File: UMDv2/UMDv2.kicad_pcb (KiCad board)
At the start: 2 copper layers, 130.8 x 83.8 mm, 112 parts, among them CON201 USB-B1HSB6, CON302 JTAG-2X10-HDR, CON303 101-00405-75, CON304 UMDv2-CONN, CON305 HDR1X2, CON306 HDR1X3, SW301 PTS645SM43SMTR92_LFS, U201 MIC5504-3.3YM5-TR, U202 TPS2115APWR, U203 TPS25921ADR, U205 AZ1117CH-3.3TRG1, U207 INA199A2DCKR, U301 STM32F413ZHT6, U302 74ALVC164245DL,118, U303 74ALVC164245DL,118, X301 ECS-80-18-30-JGN-TR

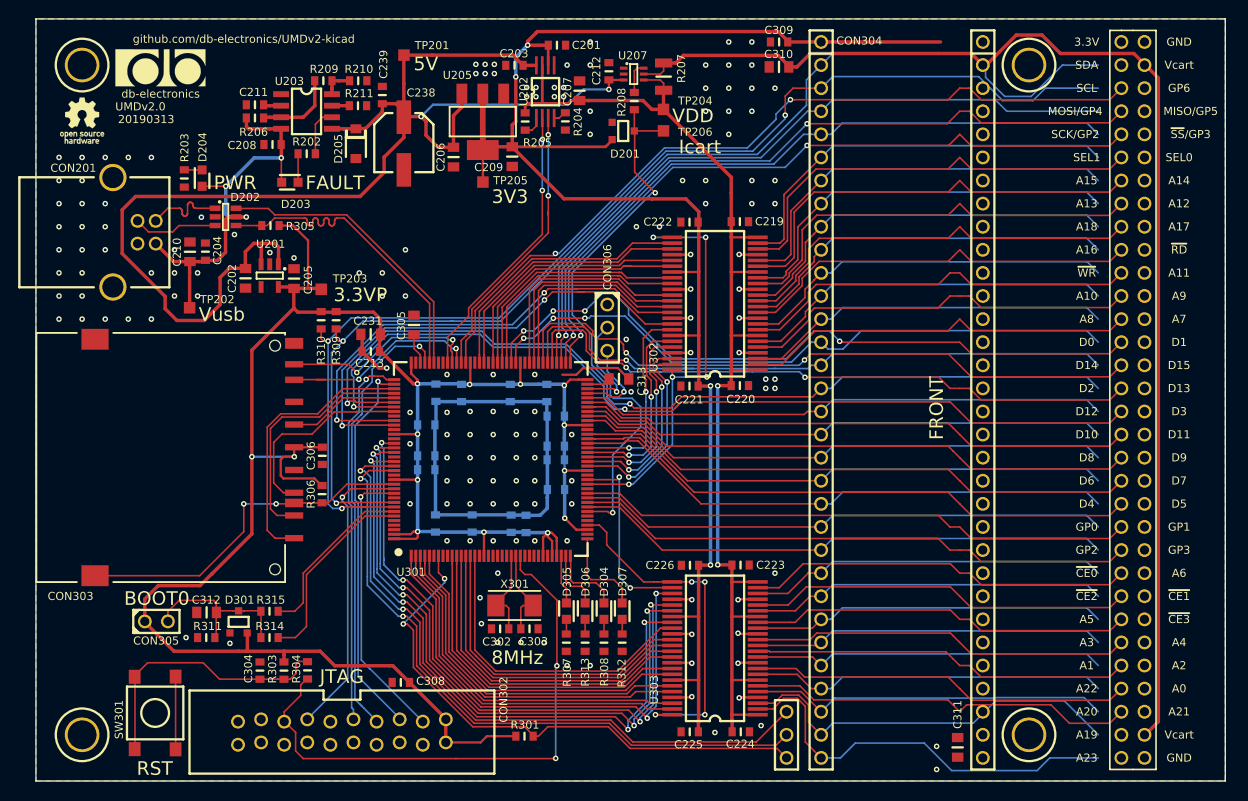
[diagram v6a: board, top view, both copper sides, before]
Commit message: added board dimensions to dwgs layer
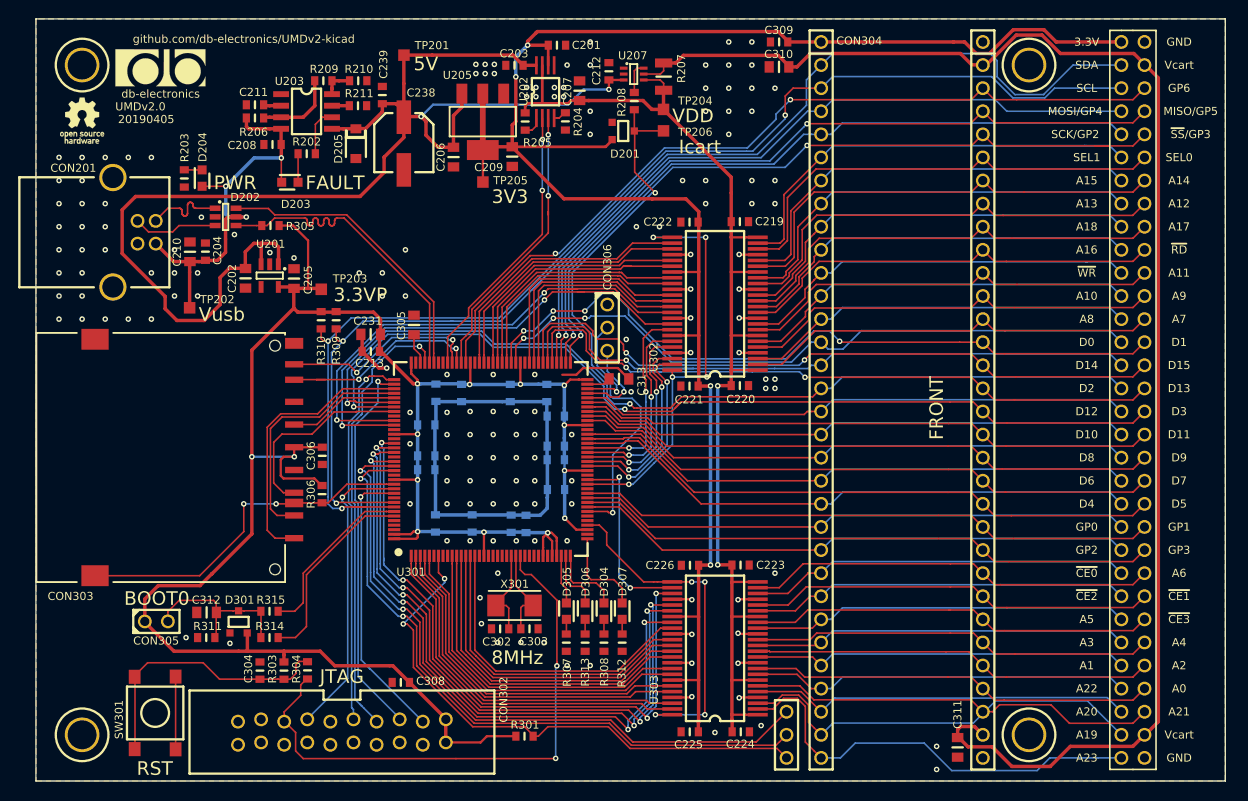
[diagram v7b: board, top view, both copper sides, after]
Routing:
- net Vcart: track 136.0 -> 163.5 mm
- net +3V3: track 183.1 -> 205.1 mm
- net /Microcontroller/SPI2_NSS: track 79.1 -> 83.3 mm
- net /Microcontroller/SCL1: track 129.9 -> 132.7 mm
- net /Microcontroller/USEL1: track 45.3 -> 48.1 mm
- net /Microcontroller/~UCE3~: track 42.0 -> 44.7 mm
- net /Microcontroller/~UWR~: track 41.3 -> 44.0 mm
- net /Microcontroller/UA21: track 42.9 -> 45.4 mm
- net /Microcontroller/UA23: track 45.5 -> 48.0 mm
- net /Microcontroller/UA19: track 43.8 -> 46.4 mm
- net /Microcontroller/SPI2_SCK: track 76.7 -> 79.2 mm
- net /Microcontroller/SPI2_MOSI: track 78.1 -> 80.6 mm
- net /Microcontroller/D8: track 59.2 -> 61.7 mm
- net /Microcontroller/D7: track 62.5 -> 65.0 mm
- net /Microcontroller/D4: track 60.2 -> 62.8 mm
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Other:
- board text added: "20190405"
- board text removed: "20190313"

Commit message: pulling the trigger on v2.0 PCB release
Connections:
- net /Microcontroller/QSPI_CLK renamed Net-(U301-Pad117)
- net /Microcontroller/QSPI_IO0 renamed Net-(U301-Pad20)
- net /Microcontroller/QSPI_IO1 renamed Net-(U301-Pad21)
- net /Microcontroller/QSPI_IO2 renamed Net-(U301-Pad19)
- net /Microcontroller/QSPI_IO3 renamed Net-(U301-Pad18)
- net /Microcontroller/QSPI_NCS renamed Net-(U301-Pad91)
- CON303 pad 11: Net-(CON303-Pad11) -> /Microcontroller/~SDWP~
- R309 pad 2: /Microcontroller/SDA1 -> /Microcontroller/SCL1
- R310 pad 2: /Microcontroller/SCL1 -> /Microcontroller/SDA1
- U301 pad 140: Net-(U301-Pad140) -> /Microcontroller/~SDWP~
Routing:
- net /Microcontroller/~SDWP~: track 0.00 -> 39.2 mm, vias 0 -> 2
- net Vusb: vias 3 -> 4
- net GND: vias 159 -> 197
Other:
- board text added: "20190408"
- board text removed: "20190405"
